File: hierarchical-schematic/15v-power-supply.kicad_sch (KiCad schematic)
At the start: 29 parts, among them J902 Terminal Block, P901 120VAC

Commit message: improvements to hierarchical schematic
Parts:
- D901, D902, D903, D904: value (none) -> 1n5060; footprint (none) -> Diode_THT:D_DO-41_SOD81_P7.62mm_Horizontal
- F901: value (none) -> 0.5A
- J901: value (none) -> Terminal Block; footprint (none) -> 15v-supply:terminal-block-691103110003
- SW901: value (none) -> SW_SPST
- T901: value (none) -> XFORMER
- U901: value (none) -> LM7815; footprint (none) -> Package_TO_SOT_THT:TO-220-3_Horizontal_TabUp
- U902: value (none) -> LM7915; footprint (none) -> Package_TO_SOT_THT:TO-220-3_Horizontal_TabUp
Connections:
- net +15 REGULATED renamed +15
- net -15 REGULATED renamed -15
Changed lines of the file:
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@@
   (junction (at 151.13 48.26) (diameter 0) (color 0 0 0 0)
   )
+  (junction (at 234.95 105.41) (diameter 0) (color 0 0 0 0)
+  )
   (junction (at 213.36 25.4) (diameter 0) (color 0 0 0 0)
   )
@@
   (junction (at 101.6 43.18) (diameter 0) (color 0 0 0 0)
   )
+  (junction (at 234.95 157.48) (diameter 0) (color 0 0 0 0)
+  )
   (junction (at 152.4 53.34) (diameter 0) (color 0 0 0 0)
   )
@@
     (stroke (width 0) (type default) (color 0 0 0 0))
   )
+  (wire (pts (xy 234.95 157.48) (xy 245.11 157.48))
+    (stroke (width 0) (type default) (color 0 0 0 0))
+  )
   (polyline (pts (xy 129.54 198.12) (xy 50.8 198.12))
     (stroke (width 0) (type default) (color 0 0 0 0))
@@
   )
   (wire (pts (xy 232.41 82.55) (xy 248.92 82.55))
+    (stroke (width 0) (type default) (color 0 0 0 0))
+  )
+  (wire (pts (xy 234.95 105.41) (xy 243.84 105.41))
     (stroke (width 0) (type default) (color 0 0 0 0))
   )
@@
     (effects (font (size 1.27 1.27)) (justify left bottom))
   )
-  (label "-15 REGULATED" (at 215.9 157.48 0)
-    (effects (font (size 1.27 1.27)) (justify left bottom))
-  )
   (label "VCC" (at 73.66 43.18 0)
     (effects (font (size 1.27 1.27)) (justify left bottom))
@@
     (effects (font (size 1.27 1.27)) (justify left bottom))
   )
-  (label "+15 REGULATED" (at 214.63 105.41 0)
-    (effects (font (size 1.27 1.27)) (justify left bottom))
-  )
   (label "7915 IN" (at 90.17 157.48 0)
     (effects (font (size 1.27 1.27)) (justify left bottom))
@@
     (effects (font (size 1.27 1.27)) (justify left bottom))
   )
+  (global_label "+15" (shape input) (at 243.84 105.41 0) (fields_autoplaced)
+    (effects (font (size 1.27 1.27)) (justify left))
+    (property "Intersheet References" "${INTERSHEET_REFS}" (id 0) (at 250.2445 105.3306 0)
+      (effects (font (size 1.27 1.27)) (justify left) hide)
+    )
+  )
+  (global_label "-15" (shape input) (at 245.11 157.48 0) (fields_autoplaced)
+    (effects (font (size 1.27 1.27)) (justify left))
+    (property "Intersheet References" "${INTERSHEET_REFS}" (id 0) (at 251.5145 157.4006 0)
+      (effects (font (size 1.27 1.27)) (justify left) hide)
+    )
+  )
   (symbol (lib_id "Device:C_Polarized_Small_US") (at 248.92 71.12 0) (unit 1)
     (in_bom yes) (on_board yes) (fields_autoplaced)
@@
     (in_bom yes) (on_board yes) (fields_autoplaced)
     (property "Reference" "U901" (id 0) (at 111.76 97.79 0))
-    (property "Value" "" (id 1) (at 111.76 100.33 0))
-    (property "Footprint" "" (id 2) (at 112.395 109.22 0)
+    (property "Value" "LM7815" (id 1) (at 111.76 100.33 0))
+    (property "Footprint" "Package_TO_SOT_THT:TO-220-3_Horizontal_TabUp" (id 2) (at 112.395 109.22 0)
       (effects (font (size 1.27 1.27) italic) (justify left) hide)
     )
@@
       (effects (font (size 1.27 1.27)) (justify left))
     )
-    (property "Value" "" (id 1) (at 158.75 52.0699 90)
-      (effects (font (size 1.27 1.27)) (justify left))
-    )
-    (property "Footprint" "" (id 2) (at 157.48 50.8 0)
+    (property "Value" "Terminal Block" (id 1) (at 158.75 52.0699 90)
+      (effects (font (size 1.27 1.27)) (justify left))
+    )
+    (property "Footprint" "15v-supply:terminal-block-691103110003" (id 2) (at 157.48 50.8 0)
       (effects (font (size 1.27 1.27)) (justify left bottom) hide)
     )
@@
       (effects (font (size 1.27 1.27)) (justify right))
     )
-    (property "Value" "" (id 1) (at 180.34 38.0999 90)
+    (property "Value" "1n5060" (id 1) (at 180.34 38.0999 90)
       (effects (font (size 1.27 1.27)) (justify right))
     )
-    (property "Footprint" "" (id 2) (at 176.53 36.83 0)
+    (property "Footprint" "Diode_THT:D_DO-41_SOD81_P7.62mm_Horizontal" (id 2) (at 176.53 36.83 0)
       (effects (font (size 1.27 1.27)) (justify left bottom) hide)
     )
@@
     (in_bom yes) (on_board no)
     (property "Reference" "F901" (id 0) (at 95.25 38.1 90))
-    (property "Value" "" (id 1) (at 95.25 40.64 90))
+    (property "Value" "0.5A" (id 1) (at 95.25 40.64 90))
     (property "Footprint" "" (id 2) (at 95.25 44.958 90)
       (effects (font (size 1.27 1.27)) hide)
@@
       (effects (font (size 1.27 1.27)) (justify right))
     )
-    (property "Value" "" (id 1) (at 217.17 72.3899 90)
+    (property "Value" "1n5060" (id 1) (at 217.17 72.3899 90)
       (effects (font (size 1.27 1.27)) (justify right))
     )
-    (property "Footprint" "" (id 2) (at 213.36 71.12 0)
+    (property "Footprint" "Diode_THT:D_DO-41_SOD81_P7.62mm_Horizontal" (id 2) (at 213.36 71.12 0)
       (effects (font (size 1.27 1.27)) (justify left bottom) hide)
     )
@@
     (in_bom yes) (on_board no) (fields_autoplaced)
     (property "Reference" "T901" (id 0) (at 123.19 35.56 0))
-    (property "Value" "" (id 1) (at 123.19 38.1 0))
+    (property "Value" "XFORMER" (id 1) (at 123.19 38.1 0))
     (property "Footprint" "" (id 2) (at 123.19 50.8 0)
       (effects (font (size 1.27 1.27)) hide)
@@
     (in_bom yes) (on_board yes) (fields_autoplaced)
     (property "Reference" "U902" (id 0) (at 111.76 149.86 0))
-    (property "Value" "" (id 1) (at 111.76 152.4 0))
-    (property "Footprint" "" (id 2) (at 111.76 152.4 0)
+    (property "Value" "LM7915" (id 1) (at 111.76 152.4 0))
+    (property "Footprint" "Package_TO_SOT_THT:TO-220-3_Horizontal_TabUp" (id 2) (at 111.76 152.4 0)
       (effects (font (size 1.27 1.27) italic) hide)
     )
@@
       (effects (font (size 1.27 1.27)) (justify right))
     )
-    (property "Value" "" (id 1) (at 217.17 38.0999 90)
+    (property "Value" "1n5060" (id 1) (at 217.17 38.0999 90)
       (effects (font (size 1.27 1.27)) (justify right))
     )
-    (property "Footprint" "" (id 2) (at 213.36 36.83 0)
+    (property "Footprint" "Diode_THT:D_DO-41_SOD81_P7.62mm_Horizontal" (id 2) (at 213.36 36.83 0)
       (effects (font (size 1.27 1.27)) (justify left bottom) hide)
     )
@@
     (in_bom yes) (on_board no) (fields_autoplaced)
     (property "Reference" "SW901" (id 0) (at 83.82 36.83 0))
-    (property "Value" "" (id 1) (at 83.82 39.37 0))
+    (property "Value" "SW_SPST" (id 1) (at 83.82 39.37 0))
     (property "Footprint" "" (id 2) (at 83.82 43.18 0)
       (effects (font (size 1.27 1.27)) hide)
@@
       (effects (font (size 1.27 1.27)) (justify right))
     )
-    (property "Value" "" (id 1) (at 180.34 72.3899 90)
+    (property "Value" "1n5060" (id 1) (at 180.34 72.3899 90)
       (effects (font (size 1.27 1.27)) (justify right))
     )
-    (property "Footprint" "" (id 2) (at 176.53 71.12 0)
-      (effects (font (size 1.27 1.27)) (justify left bottom) hide)
-    )
+    (property "Footprint" "Diode_THT:D_DO-41_SOD81_P7.62mm_Horizontal" (id 2) (at 176.53 71.12 0)
+      (effects (font (size 1.27 1.27)) (justify left bottom) hide)
+    )

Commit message: 2ndmixer-2ndlo
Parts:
- removed C904, C905: 6.8u, Capacitor_THT:CP_Radial_D5.0mm_P2.50mm, symbol Device:C_Small
- added C904, C905: 6.8u, Capacitor_THT:CP_Radial_D8.0mm_P3.50mm, symbol Device:C_Polarized_Small_US
- D901, D902, D903, D904: Spice_Lib_File 15v-supply\15v-supply-spice\1n5060.lib -> 15v-supply-spice/1n5060.lib; Spice_Node_Sequence (none) -> 2 1
- H901, H902, H903, H904: Spice_Netlist_Enabled (none) -> N; Spice_Primitive (none) -> R
- T901: Spice_Lib_File 15v-supply\15v-supply-spice\xformer.lib -> 15v-supply-spice/xformer.lib
- U901, U902: Spice_Lib_File 15v-supply\15v-supply-spice\regulators.lib -> 15v-supply-spice/regulators.lib
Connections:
- net 7815 IN: now also D901.1 (Cathode), D903.1 (Cathode); no longer D901.2 (Anode), D903.2 (Anode)
- net 7915 IN: now also D902.2 (Anode), D904.2 (Anode); no longer D902.1 (Cathode), D904.1 (Cathode)
- net GND: now also C904.2, C905.1
- net TRAN OUT1: now also D901.2 (Anode); no longer D901.1 (Cathode), D902.2 (Anode)
- net TRAN OUT2: now also D902.1 (Cathode), D903.2 (Anode), D904.1 (Cathode); no longer D903.1 (Cathode), D904.2 (Anode)
- net +15 renamed +15 Regulated
- net +15 Regulated: now also C904.1
- net -15 renamed -15 Regulated
- net -15 Regulated: now also C905.2
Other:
- note added: "250V"
- note added: "50V"
- note added: "C904, C905 = 35V, Tantalum"
- note removed: "C10, C11 = 35V, Tantalum"
- note removed: "COMMON"

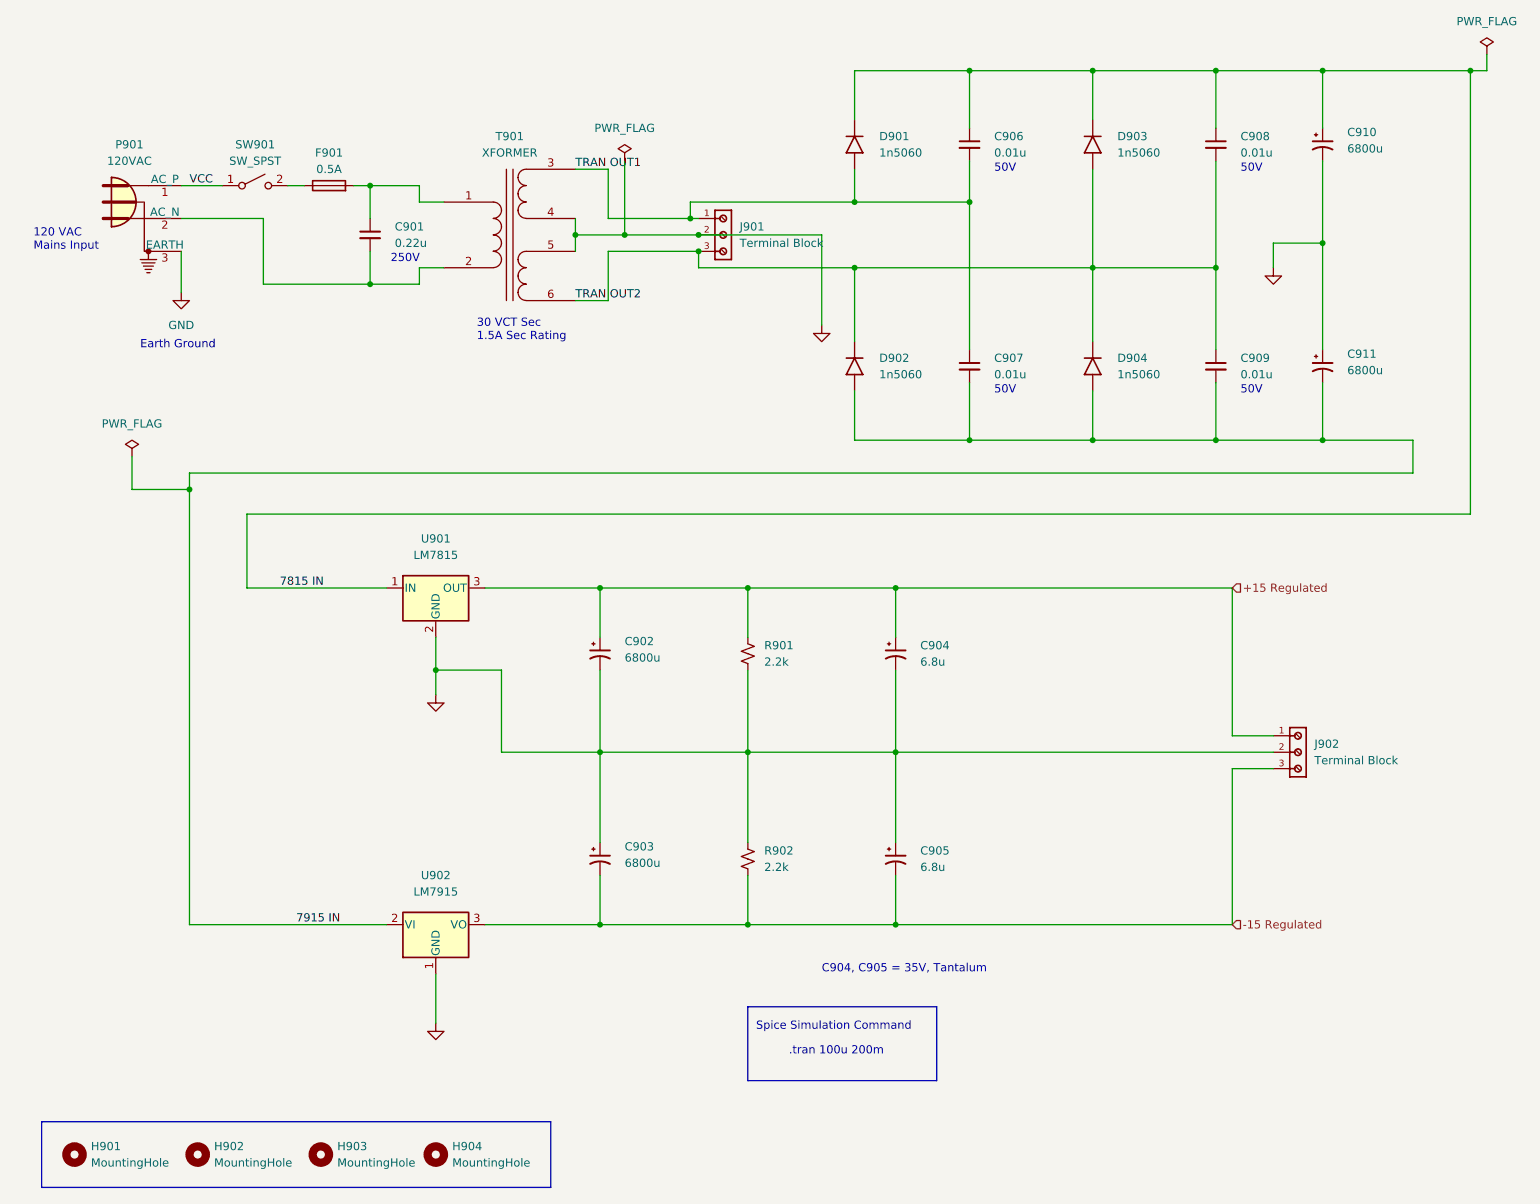
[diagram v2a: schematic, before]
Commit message: improved if and log amp and second lo/mixer
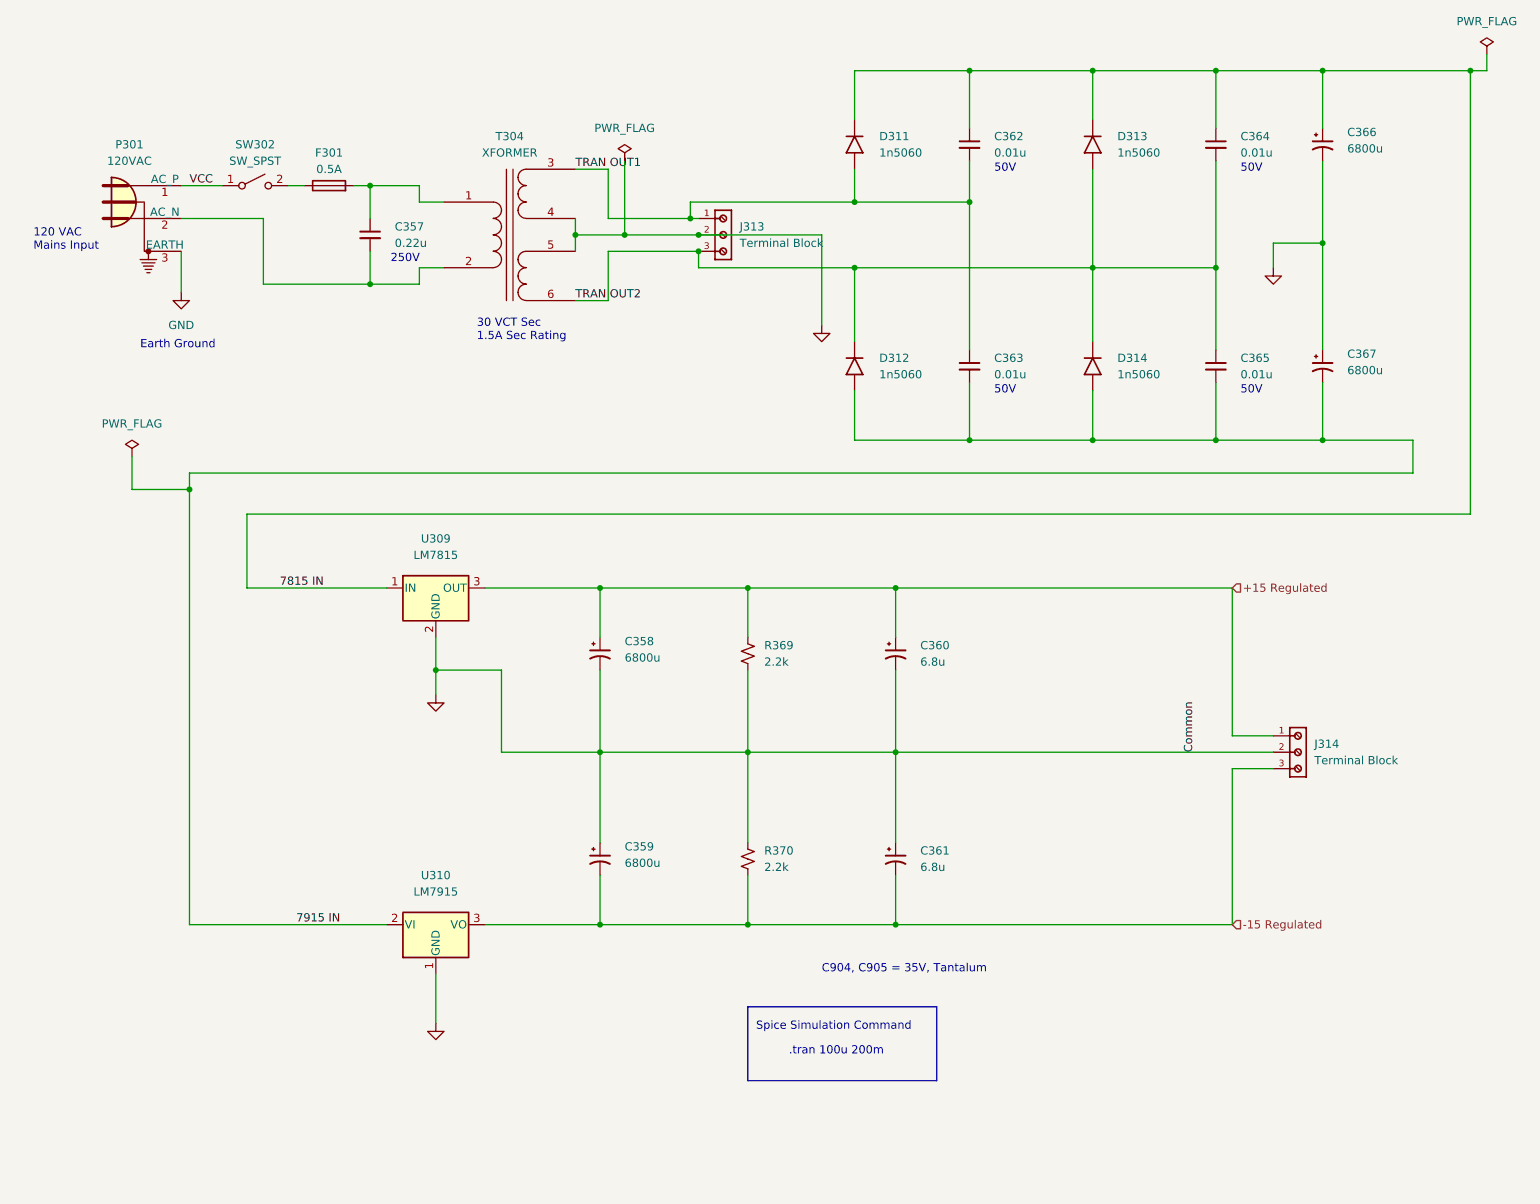
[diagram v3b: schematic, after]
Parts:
- removed H901, H902, H903, H904: MountingHole, MountingHole:MountingHole_3.2mm_M3, symbol Mechanical:MountingHole
- renumbered C901 to C357, C902 to C358, C903 to C359, C904 to C360, C905 to C361, C906 to C362, C907 to C363, C908 to C364, C909 to C365, C910 to C366, C911 to C367, D901 to D311, D902 to D312, D903 to D313, D904 to D314, F901 to F301, J901 to J313, J902 to J314, P901 to P301, R901 to R369, R902 to R370, SW901 to SW302, T901 to T304, U901 to U309, U902 to U310

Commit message: Hierarchical schematic updates
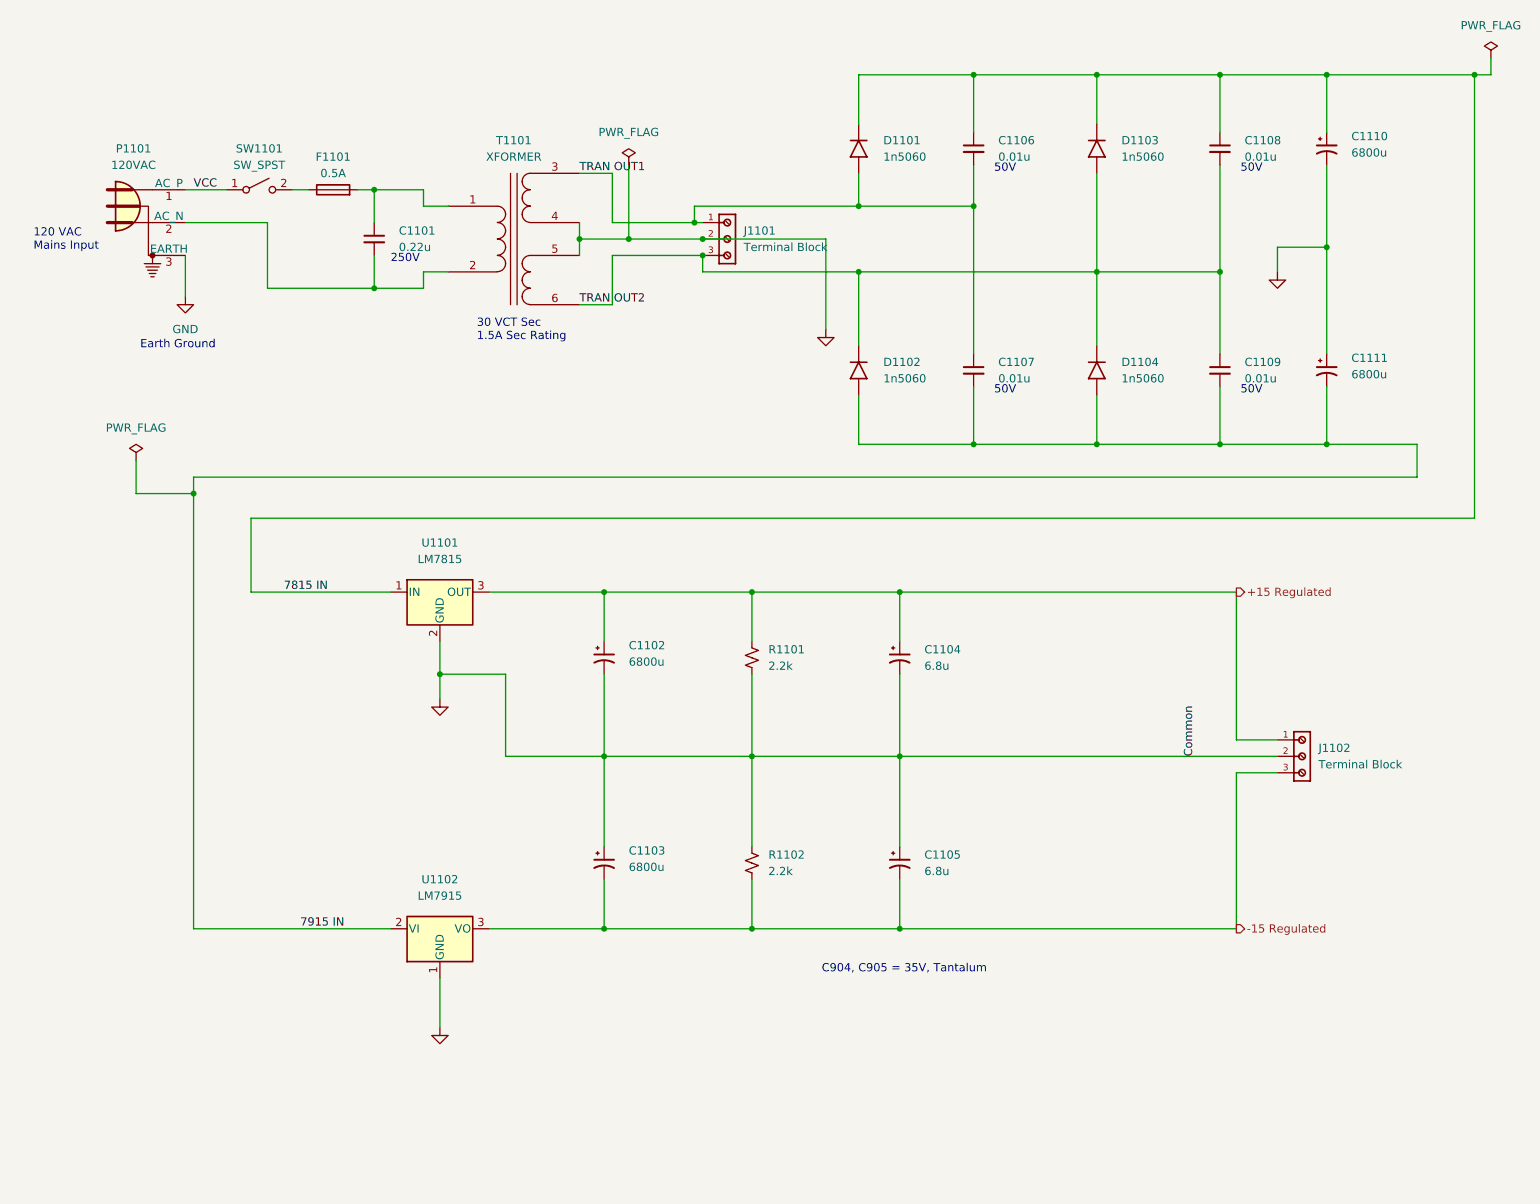
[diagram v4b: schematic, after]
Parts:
- renumbered C357 to C1101, C358 to C1102, C359 to C1103, C360 to C1104, C361 to C1105, C362 to C1106, C363 to C1107, C364 to C1108, C365 to C1109, C366 to C1110, C367 to C1111, D311 to D1101, D312 to D1102, D313 to D1103, D314 to D1104, F301 to F1101, J313 to J1101, J314 to J1102, P301 to P1101, R369 to R1101, R370 to R1102, SW302 to SW1101, T304 to T1101, U309 to U1101, U310 to U1102
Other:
- note removed: ".tran 100u 200m"
- note removed: "Spice Simulation Command"
- title: 15 Volt Power Supply -> Spectrum Analyzer: 15 Volt Power Supply
- moved on the sheet: C1101, C1102, C1103, C1104, C1105, C1106, C1107, C1108, C1109, C1110, C1111, D1101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
